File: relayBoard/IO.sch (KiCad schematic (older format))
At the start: 15 parts, among them IC1 ADUM1251, J13 Conn_02x07_Odd_Even, J14 Conn_02x07_Odd_Even, U1 PCA9555APW,118, U2 PCA9555APW,118, U3 PCA9555APW,118, U4 PCA9555APW,118

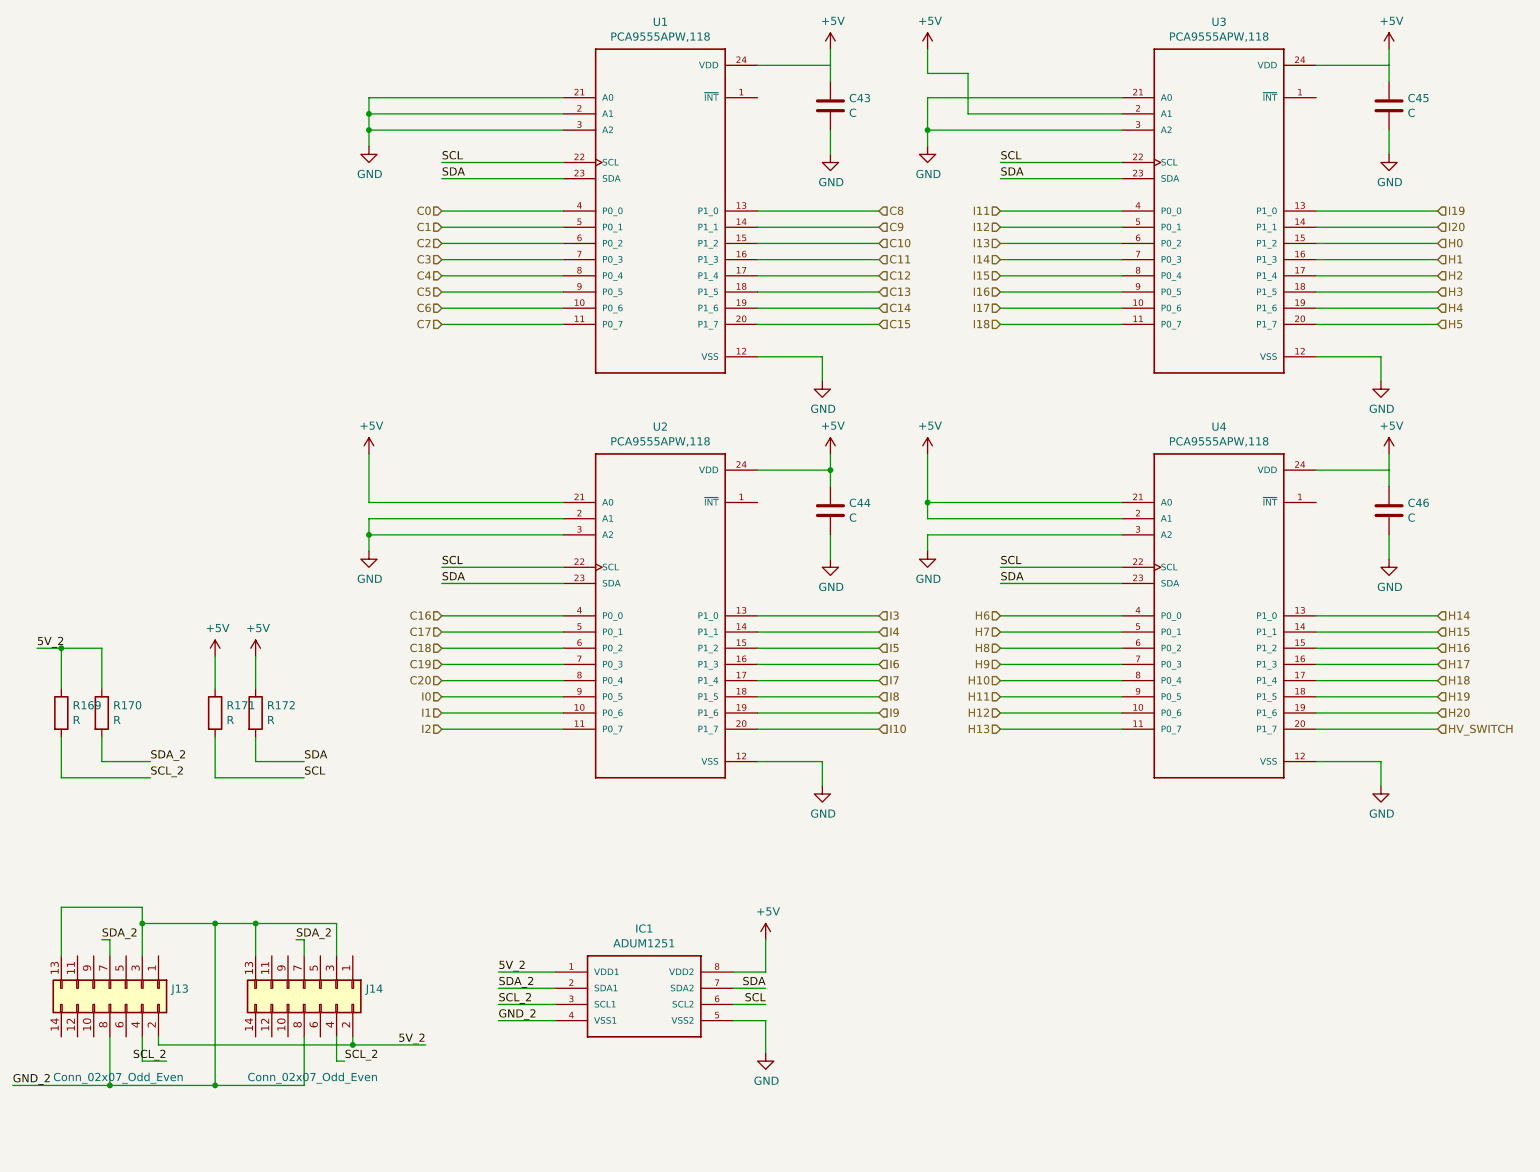
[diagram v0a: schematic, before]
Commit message: Third pass, fixing footprints to match JLC components
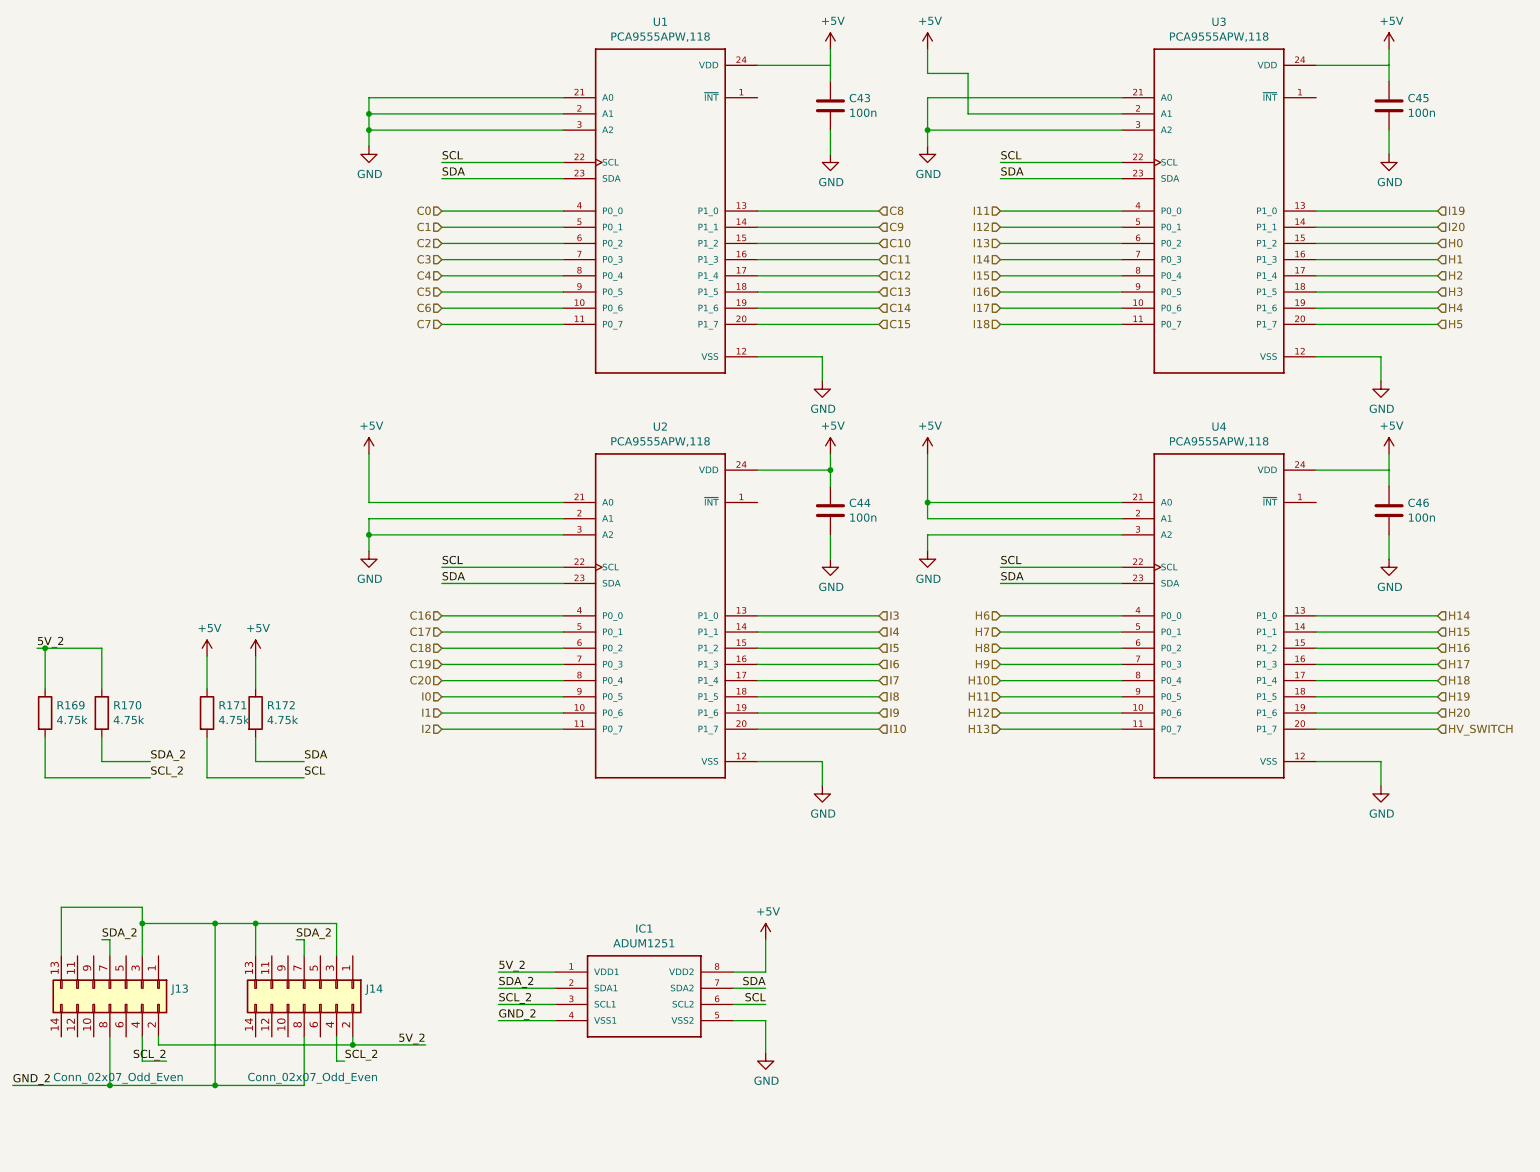
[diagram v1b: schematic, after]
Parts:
- C43, C44, C45, C46: value C -> 100n
- R169, R170, R171, R172: value R -> 4.75k
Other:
- moved on the sheet: R169, R171
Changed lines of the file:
@@
 P 5700 3650
 F 0 "C44" H 5815 3696 50  0000 L CNN
-F 1 "C" H 5815 3605 50  0000 L CNN
+F 1 "100n" H 5815 3605 50  0000 L CNN
 F 2 "Resistor_SMD:R_0603_1608Metric" H 5738 3500 50  0001 C CNN
 F 3 "~" H 5700 3650 50  0001 C CNN
@@
 P 5700 1150
 F 0 "C43" H 5815 1196 50  0000 L CNN
-F 1 "C" H 5815 1105 50  0000 L CNN
+F 1 "100n" H 5815 1105 50  0000 L CNN
 F 2 "Resistor_SMD:R_0603_1608Metric" H 5738 1000 50  0001 C CNN
 F 3 "~" H 5700 1150 50  0001 C CNN
@@
 P 9150 1150
 F 0 "C45" H 9265 1196 50  0000 L CNN
-F 1 "C" H 9265 1105 50  0000 L CNN
+F 1 "100n" H 9265 1105 50  0000 L CNN
 F 2 "Resistor_SMD:R_0603_1608Metric" H 9188 1000 50  0001 C CNN
 F 3 "~" H 9150 1150 50  0001 C CNN
@@
 P 9150 3650
 F 0 "C46" H 9265 3696 50  0000 L CNN
-F 1 "C" H 9265 3605 50  0000 L CNN
+F 1 "100n" H 9265 3605 50  0000 L CNN
 F 2 "Resistor_SMD:R_0603_1608Metric" H 9188 3500 50  0001 C CNN
 F 3 "~" H 9150 3650 50  0001 C CNN
@@
 L Device:R R169
 U 1 1 6249580E
-P 950 4900
-F 0 "R169" H 1020 4946 50  0000 L CNN
-F 1 "R" H 1020 4855 50  0000 L CNN
-F 2 "Resistor_SMD:R_0603_1608Metric" V 880 4900 50  0001 C CNN
-F 3 "~" H 950 4900 50  0001 C CNN
-	1    950  4900
+P 850 4900
+F 0 "R169" H 920 4946 50  0000 L CNN
+F 1 "4.75k" H 920 4855 50  0000 L CNN
+F 2 "Resistor_SMD:R_0603_1608Metric" V 780 4900 50  0001 C CNN
+F 3 "~" H 850 4900 50  0001 C CNN
+	1    850  4900
 	1    0    0    -1
 $EndComp
@@
 P 1200 4900
 F 0 "R170" H 1270 4946 50  0000 L CNN
-F 1 "R" H 1270 4855 50  0000 L CNN
+F 1 "4.75k" H 1270 4855 50  0000 L CNN
 F 2 "Resistor_SMD:R_0603_1608Metric" V 1130 4900 50  0001 C CNN
 F 3 "~" H 1200 4900 50  0001 C CNN
@@
 L Device:R R171
 U 1 1 6249E42A
-P 1900 4900
-F 0 "R171" H 1970 4946 50  0000 L CNN
-F 1 "R" H 1970 4855 50  0000 L CNN
-F 2 "Resistor_SMD:R_0603_1608Metric" V 1830 4900 50  0001 C CNN
-F 3 "~" H 1900 4900 50  0001 C CNN
-	1    1900 4900
+P 1850 4900
+F 0 "R171" H 1920 4946 50  0000 L CNN
+F 1 "4.75k" H 1920 4855 50  0000 L CNN
+F 2 "Resistor_SMD:R_0603_1608Metric" V 1780 4900 50  0001 C CNN
+F 3 "~" H 1850 4900 50  0001 C CNN
+	1    1850 4900
 	1    0    0    -1
 $EndComp
@@
 P 2150 4900
 F 0 "R172" H 2220 4946 50  0000 L CNN
-F 1 "R" H 2220 4855 50  0000 L CNN
+F 1 "4.75k" H 2220 4855 50  0000 L CNN
 F 2 "Resistor_SMD:R_0603_1608Metric" V 2080 4900 50  0001 C CNN
 F 3 "~" H 2150 4900 50  0001 C CNN
@@
 $EndComp
 Wire Wire Line
-	1900 4750 1900 4550
+	1850 4750 1850 4550
 $Comp
 L power:+5V #PWR015
 U 1 1 624C8110
-P 1900 4550
-F 0 "#PWR015" H 1900 4400 50  0001 C CNN
-F 1 "+5V" H 1915 4723 50  0000 C CNN
-F 2 "" H 1900 4550 50  0001 C CNN
-F 3 "" H 1900 4550 50  0001 C CNN
-	1    1900 4550
-	1    0    0    -1
-$EndComp
-Wire Wire Line
-	1900 5050 1900 5300
-Wire Wire Line
-	1900 5300 2450 5300
+P 1850 4550
+F 0 "#PWR015" H 1850 4400 50  0001 C CNN
+F 1 "+5V" H 1865 4723 50  0000 C CNN
+F 2 "" H 1850 4550 50  0001 C CNN
+F 3 "" H 1850 4550 50  0001 C CNN
+	1    1850 4550
+	1    0    0    -1
+$EndComp
 Wire Wire Line
 	2150 5050 2150 5200
@@
 	2150 5200 2450 5200
 Wire Wire Line
-	950  5050 950  5300
-Wire Wire Line
-	950  5300 1500 5300
-Wire Wire Line
 	1200 5050 1200 5200
 Wire Wire Line
@@
 Wire Wire Line
 	1200 4750 1200 4500
-Wire Wire Line
-	1200 4500 950  4500
-Wire Wire Line
-	950  4750 950  4500
-Connection ~ 950  4500
-Wire Wire Line
-	950  4500 800  4500
 Text Label 800  4500 0    50   ~ 0
 5V_2
@@
 Text HLabel 9450 5000 2    50   Input ~ 0
 HV_SWITCH
+Wire Wire Line
+	850  4750 850  4500
+Connection ~ 850  4500
+Wire Wire Line
+	850  4500 800  4500
+Wire Wire Line
+	850  5050 850  5300
+Wire Wire Line
+	850  5300 1500 5300
+Wire Wire Line
+	850  4500 1200 4500
+Wire Wire Line
+	1850 5050 1850 5300
+Wire Wire Line
+	1850 5300 2450 5300
 $EndSCHEMATC

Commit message: Cuyler's revisions to the relay board
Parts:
- IC1: symbol ADUM1251:ADUM1251 -> relayBoard-rescue:ADUM1251-ADUM1251
- U1, U2, U3, U4: symbol PCA9555APW_118:PCA9555APW,118 -> relayBoard-rescue:PCA9555APW,118-PCA9555APW_118
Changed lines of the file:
@@
 EESchema Schematic File Version 4
-EELAYER 30 0
+LIBS:relayBoard-cache
+EELAYER 29 0
 EELAYER END
 $Descr A4 11693 8268
@@
 	2450 6300 2450 6400
 $Comp
-L PCA9555APW_118:PCA9555APW,118 U3
+L relayBoard-rescue:PCA9555APW,118-PCA9555APW_118 U3
 U 1 1 5F2E43EB
 P 8100 1800
@@
 SDA
 $Comp
-L PCA9555APW_118:PCA9555APW,118 U4
+L relayBoard-rescue:PCA9555APW,118-PCA9555APW_118 U4
 U 1 1 5F2F0FD4
 P 8100 4300
@@
 SDA
 $Comp
-L PCA9555APW_118:PCA9555APW,118 U1
+L relayBoard-rescue:PCA9555APW,118-PCA9555APW_118 U1
 U 1 1 5F2FB338
 P 4650 1800
@@
 SDA
 $Comp
-L PCA9555APW_118:PCA9555APW,118 U2
+L relayBoard-rescue:PCA9555APW,118-PCA9555APW_118 U2
 U 1 1 5F3066B6
 P 4650 4300
@@
 Connection ~ 6300 3600
 $Comp
-L ADUM1251:ADUM1251 IC1
+L relayBoard-rescue:ADUM1251-ADUM1251 IC1
 U 1 1 5F3CF351
 P 4200 6900

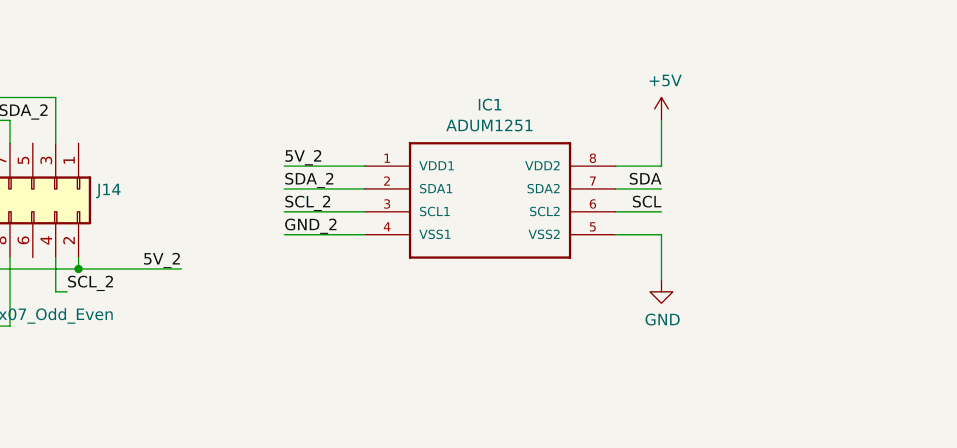
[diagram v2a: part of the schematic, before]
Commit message: updates to connector connections and converter transformer
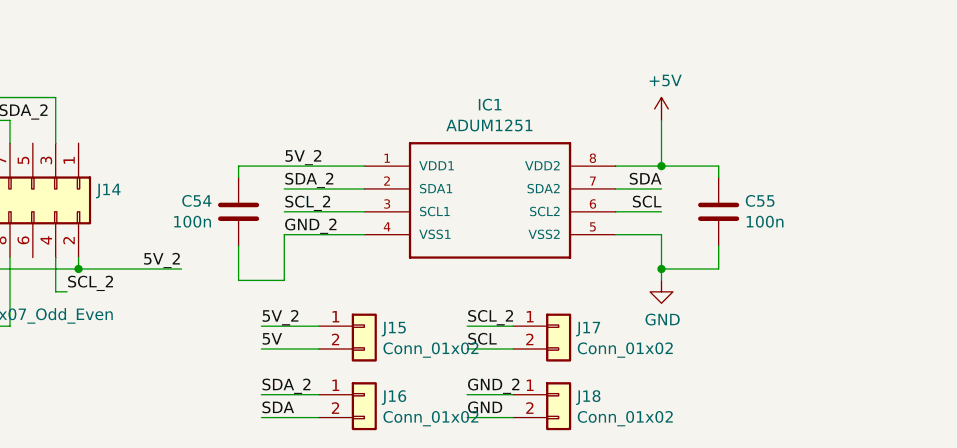
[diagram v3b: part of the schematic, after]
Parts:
- added C54, C55: 100n, Resistor_SMD:R_0603_1608Metric, symbol Device:C
- added J15, J16, J17, J18: Conn_01x02, Connector_PinHeader_2.00mm:PinHeader_1x02_P2.00mm_Vertical, symbol Connector_Generic:Conn_01x02
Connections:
- net +5V: now also C55.1
- net 5V_2: now also C54.1, J15.1 (Pin_1)
- net GND: now also C55.2, J18.2 (Pin_2)
- net GND_2: now also C54.2, J18.1 (Pin_1)
- net SCL: now also J17.2 (Pin_2)
- net SCL_2: now also J17.1 (Pin_1)
- net SDA: now also J16.2 (Pin_2)
- net SDA_2: now also J16.1 (Pin_1)
- new net 5V: J15.2 (Pin_2)
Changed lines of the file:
@@
 EESchema Schematic File Version 4
-LIBS:relayBoard-cache
-EELAYER 29 0
+EELAYER 30 0
 EELAYER END
 $Descr A4 11693 8268
@@
 	5100 6800 5300 6800
 Wire Wire Line
-	5300 6800 5300 7000
+	5300 6800 5300 6950
 $Comp
 L power:GND #PWR021
@@
 	1    0    0    -1
 $EndComp
-Wire Wire Line
-	3650 6500 4000 6500
 Text Label 3650 6500 0    50   ~ 0
 5V_2
@@
 Wire Wire Line
 	1850 5300 2450 5300
+$Comp
+L Device:C C54
+U 1 1 5F83F5A9
+P 3450 6700
+F 0 "C54" H 3565 6746 50  0000 L CNN
+F 1 "100n" H 3565 6655 50  0000 L CNN
+F 2 "Resistor_SMD:R_0603_1608Metric" H 3488 6550 50  0001 C CNN
+F 3 "~" H 3450 6700 50  0001 C CNN
+	1    3450 6700
+	-1   0    0    -1
+$EndComp
+Wire Wire Line
+	3450 6850 3450 7000
+Wire Wire Line
+	3450 6500 4000 6500
+Wire Wire Line
+	3450 6500 3450 6550
+Wire Wire Line
+	3650 6800 3650 7000
+Wire Wire Line
+	3650 7000 3450 7000
+$Comp
+L Device:C C55
+U 1 1 5F8681FC
+P 5550 6700
+F 0 "C55" H 5665 6746 50  0000 L CNN
+F 1 "100n" H 5665 6655 50  0000 L CNN
+F 2 "Resistor_SMD:R_0603_1608Metric" H 5588 6550 50  0001 C CNN
+F 3 "~" H 5550 6700 50  0001 C CNN
+	1    5550 6700
+	1    0    0    -1
+$EndComp
+Wire Wire Line
+	5550 6850 5550 6950
+Wire Wire Line
+	5300 6500 5550 6500
+Wire Wire Line
+	5550 6500 5550 6550
+Connection ~ 5300 6500
+Wire Wire Line
+	5300 6950 5550 6950
+Connection ~ 5300 6950
+Wire Wire Line
+	5300 6950 5300 7000
+$Comp
+L Connector_Generic:Conn_01x02 J15
+U 1 1 5F8883E9
+P 4000 7200
+F 0 "J15" H 4080 7192 50  0000 L CNN
+F 1 "Conn_01x02" H 4080 7101 50  0000 L CNN
+F 2 "Connector_PinHeader_2.00mm:PinHeader_1x02_P2.00mm_Vertical" H 4000 7200 50  0001 C CNN
+F 3 "~" H 4000 7200 50  0001 C CNN
+	1    4000 7200
+	1    0    0    -1
+$EndComp
+$Comp
+L Connector_Generic:Conn_01x02 J16
+U 1 1 5F888D50
+P 4000 7500
+F 0 "J16" H 4080 7492 50  0000 L CNN
+F 1 "Conn_01x02" H 4080 7401 50  0000 L CNN
+F 2 "Connector_PinHeader_2.00mm:PinHeader_1x02_P2.00mm_Vertical" H 4000 7500 50  0001 C CNN
+F 3 "~" H 4000 7500 50  0001 C CNN
+	1    4000 7500
+	1    0    0    -1
+$EndComp
+$Comp
+L Connector_Generic:Conn_01x02 J17
+U 1 1 5F89391B
+P 4850 7200
+F 0 "J17" H 4930 7192 50  0000 L CNN
+F 1 "Conn_01x02" H 4930 7101 50  0000 L CNN
+F 2 "Connector_PinHeader_2.00mm:PinHeader_1x02_P2.00mm_Vertical" H 4850 7200 50  0001 C CNN
+F 3 "~" H 4850 7200 50  0001 C CNN
+	1    4850 7200
+	1    0    0    -1
+$EndComp
+$Comp
+L Connector_Generic:Conn_01x02 J18
+U 1 1 5F89E388
+P 4850 7500
+F 0 "J18" H 4930 7492 50  0000 L CNN
+F 1 "Conn_01x02" H 4930 7401 50  0000 L CNN
+F 2 "Connector_PinHeader_2.00mm:PinHeader_1x02_P2.00mm_Vertical" H 4850 7500 50  0001 C CNN
+F 3 "~" H 4850 7500 50  0001 C CNN
+	1    4850 7500
+	1    0    0    -1
+$EndComp
+Wire Wire Line
+	3550 7200 3800 7200
+Wire Wire Line
+	3800 7300 3550 7300
+Wire Wire Line
+	3800 7500 3550 7500
+Wire Wire Line
+	3800 7600 3550 7600
+Wire Wire Line
+	4650 7200 4450 7200
+Wire Wire Line
+	4650 7300 4450 7300
+Wire Wire Line
+	4650 7500 4450 7500
+Wire Wire Line
+	4650 7600 4450 7600
+Text Label 3550 7200 0    50   ~ 0
+5V_2
+Text Label 3550 7300 0    50   ~ 0
+5V
+Text Label 3550 7500 0    50   ~ 0
+SDA_2
+Text Label 3550 7600 0    50   ~ 0
+SDA
+Text Label 4450 7200 0    50   ~ 0
+SCL_2
+Text Label 4450 7300 0    50   ~ 0
+SCL
+Text Label 4450 7500 0    50   ~ 0
+GND_2
+Text Label 4450 7600 0    50   ~ 0
+GND
 $EndSCHEMATC
